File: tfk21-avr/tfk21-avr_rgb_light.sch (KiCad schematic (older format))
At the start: 12 parts

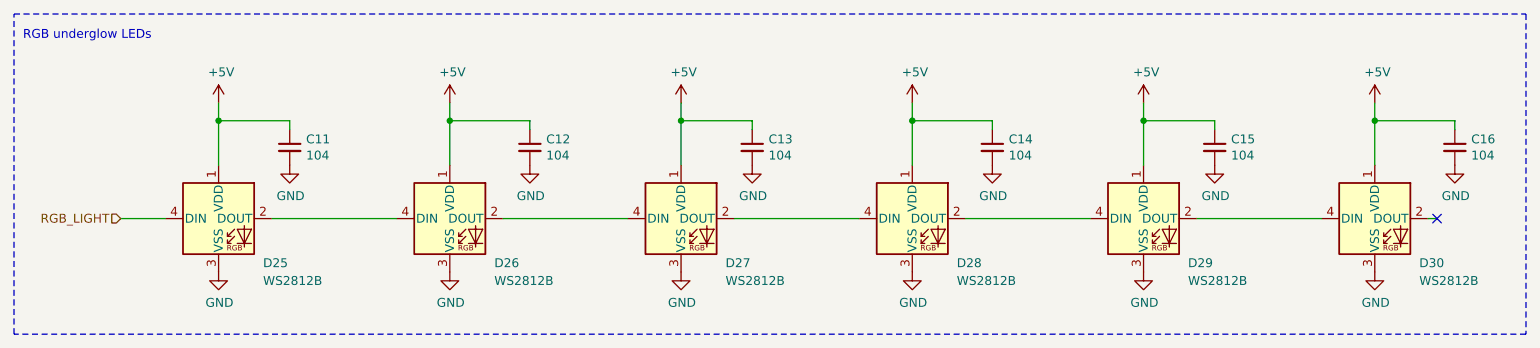
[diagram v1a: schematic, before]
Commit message: Tweak component values
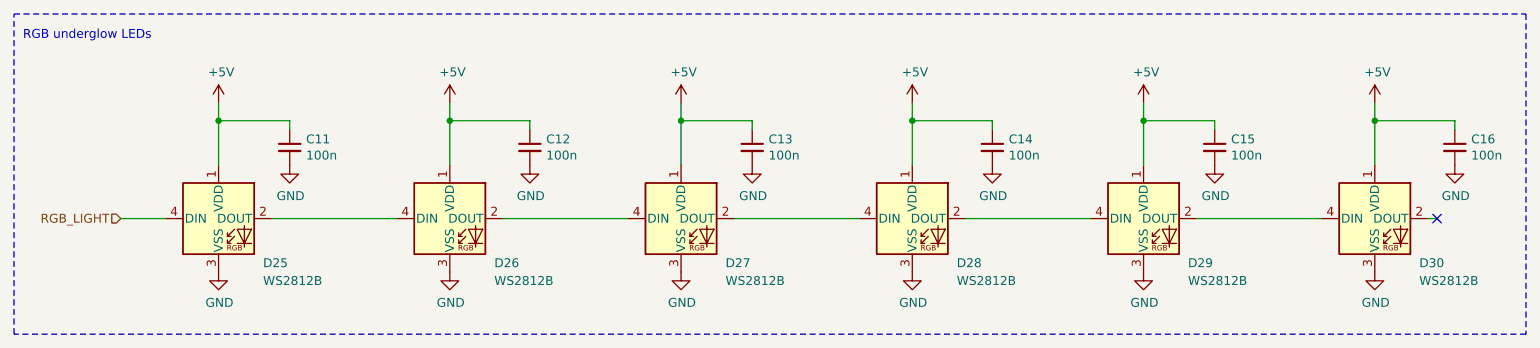
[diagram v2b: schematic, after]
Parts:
- C11, C12, C13, C14, C15, C16: value 104 -> 100n
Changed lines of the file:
@@
 AR Path="/602C340B/601B5D07" Ref="C11"  Part="1"
 F 0 "C11" H 3142 3796 50  0000 L CNN
-F 1 "104" H 3142 3705 50  0000 L CNN
+F 1 "100n" H 3142 3705 50  0000 L CNN
 F 2 "Capacitor_SMD:C_0805_2012Metric_Pad1.18x1.45mm_HandSolder" H 3050 3750 50  0001 C CNN
 F 3 "~" H 3050 3750 50  0001 C CNN
@@
 AR Path="/602C340B/601B5D2A" Ref="C12"  Part="1"
 F 0 "C12" H 4492 3796 50  0000 L CNN
-F 1 "104" H 4492 3705 50  0000 L CNN
+F 1 "100n" H 4492 3705 50  0000 L CNN
 F 2 "Capacitor_SMD:C_0805_2012Metric_Pad1.18x1.45mm_HandSolder" H 4400 3750 50  0001 C CNN
 F 3 "~" H 4400 3750 50  0001 C CNN
@@
 AR Path="/602C340B/601B5D4C" Ref="C13"  Part="1"
 F 0 "C13" H 5742 3796 50  0000 L CNN
-F 1 "104" H 5742 3705 50  0000 L CNN
+F 1 "100n" H 5742 3705 50  0000 L CNN
 F 2 "Capacitor_SMD:C_0805_2012Metric_Pad1.18x1.45mm_HandSolder" H 5650 3750 50  0001 C CNN
 F 3 "~" H 5650 3750 50  0001 C CNN
@@
 AR Path="/602C340B/601B5D6F" Ref="C14"  Part="1"
 F 0 "C14" H 7092 3796 50  0000 L CNN
-F 1 "104" H 7092 3705 50  0000 L CNN
+F 1 "100n" H 7092 3705 50  0000 L CNN
 F 2 "Capacitor_SMD:C_0805_2012Metric_Pad1.18x1.45mm_HandSolder" H 7000 3750 50  0001 C CNN
 F 3 "~" H 7000 3750 50  0001 C CNN
@@
 AR Path="/602C340B/60DF2224" Ref="C15"  Part="1"
 F 0 "C15" H 8342 3796 50  0000 L CNN
-F 1 "104" H 8342 3705 50  0000 L CNN
+F 1 "100n" H 8342 3705 50  0000 L CNN
 F 2 "Capacitor_SMD:C_0805_2012Metric_Pad1.18x1.45mm_HandSolder" H 8250 3750 50  0001 C CNN
 F 3 "~" H 8250 3750 50  0001 C CNN
@@
 AR Path="/602C340B/60DF2247" Ref="C16"  Part="1"
 F 0 "C16" H 9692 3796 50  0000 L CNN
-F 1 "104" H 9692 3705 50  0000 L CNN
+F 1 "100n" H 9692 3705 50  0000 L CNN
 F 2 "Capacitor_SMD:C_0805_2012Metric_Pad1.18x1.45mm_HandSolder" H 9600 3750 50  0001 C CNN
 F 3 "~" H 9600 3750 50  0001 C CNN
